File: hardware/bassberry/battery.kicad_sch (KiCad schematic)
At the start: 15 parts, among them J401 3S BMS module (B-,B1,B2,B+,P-), J402 NTC 10k B3380 on cell

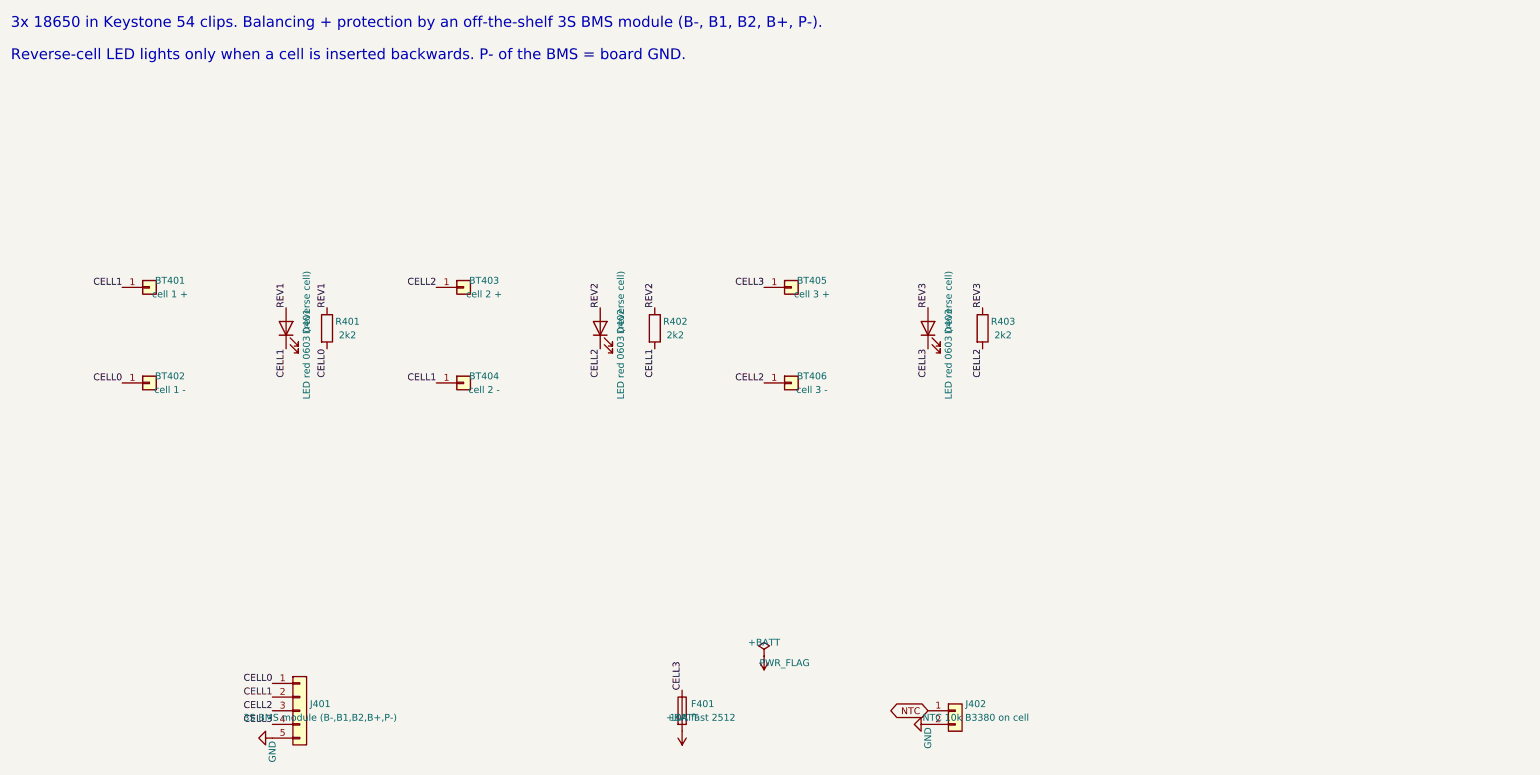
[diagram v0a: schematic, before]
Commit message: rev 0.2 board: routed with srouter, DRC 0 errors / 0 unconnected / 0 parity, digital twin 1-4 PASS; KiCad files, reports, renders
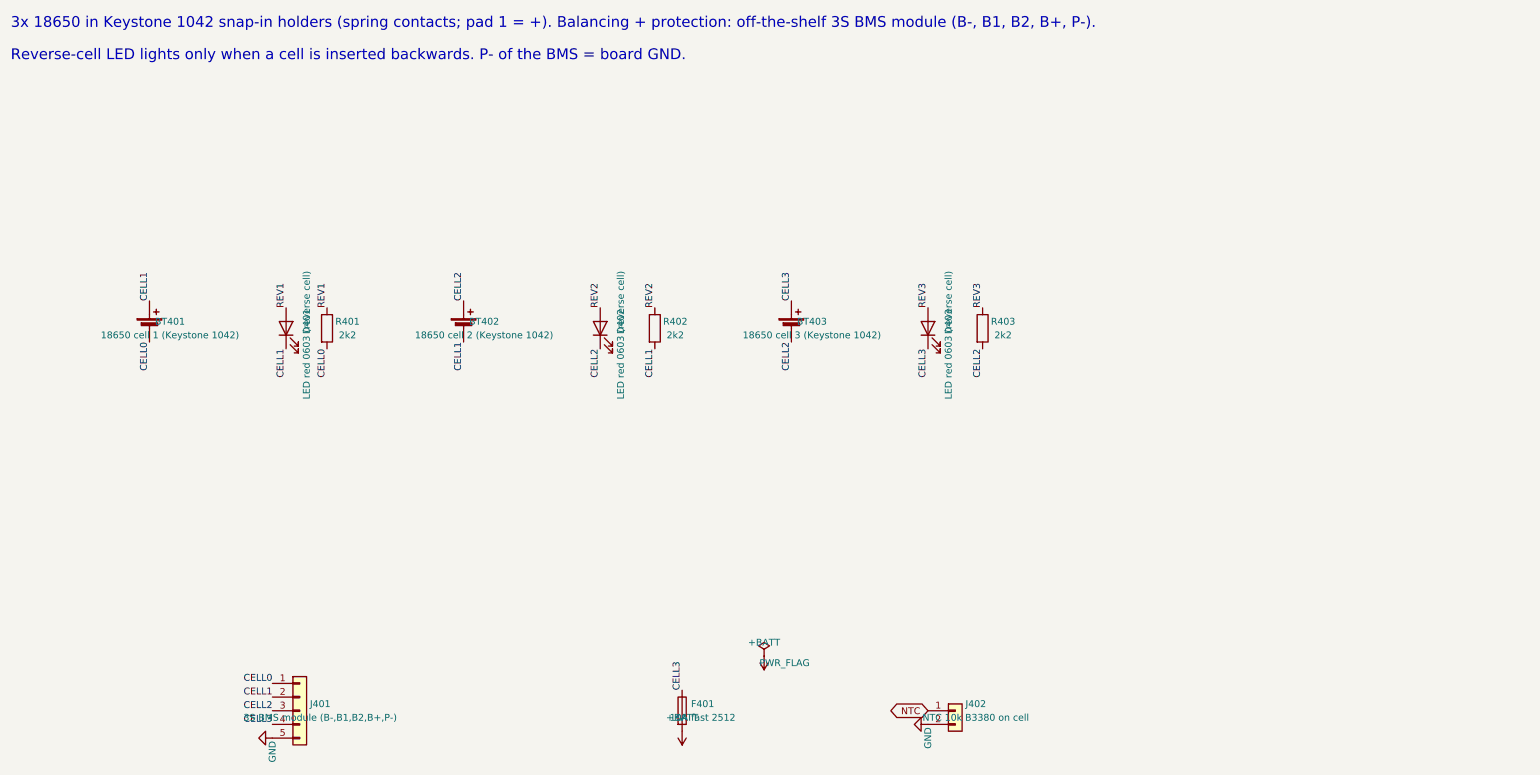
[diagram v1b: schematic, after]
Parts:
- removed BT404: cell 2 -, Battery:BatteryClip_Keystone_54_D16-19mm, symbol Connector_Generic:Conn_01x01
- removed BT405: cell 3 +, Battery:BatteryClip_Keystone_54_D16-19mm, symbol Connector_Generic:Conn_01x01
- removed BT406: cell 3 -, Battery:BatteryClip_Keystone_54_D16-19mm, symbol Connector_Generic:Conn_01x01
- BT401: value cell 1 + -> 18650 cell 1 (Keystone 1042); footprint Battery:BatteryClip_Keystone_54_D16-19mm -> Battery:BatteryHolder_Keystone_1042_1x18650; symbol Connector_Generic:Conn_01x01 -> Device:Battery_Cell
- BT402: value cell 1 - -> 18650 cell 2 (Keystone 1042); footprint Battery:BatteryClip_Keystone_54_D16-19mm -> Battery:BatteryHolder_Keystone_1042_1x18650; symbol Connector_Generic:Conn_01x01 -> Device:Battery_Cell
- BT403: value cell 2 + -> 18650 cell 3 (Keystone 1042); footprint Battery:BatteryClip_Keystone_54_D16-19mm -> Battery:BatteryHolder_Keystone_1042_1x18650; symbol Connector_Generic:Conn_01x01 -> Device:Battery_Cell
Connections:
- net CELL0: now also BT401.2 (-); no longer BT402.1 (Pin_1)
- net CELL1: now also BT402.2 (-)
- net CELL2: now also BT402.1 (+), BT403.2 (-); no longer BT403.1 (Pin_1)
- net CELL3: now also BT403.1 (+)
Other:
- note added: "3x 18650 in Keystone 1042 snap-in holders (spring contacts; pad 1 = +). Balancing + protection: off-the-shelf 3S BMS module (B-, B1, B2, B+, P-)."
- note removed: "3x 18650 in Keystone 54 clips. Balancing + protection by an off-the-shelf 3S BMS module (B-, B1, B2, B+, P-)."
